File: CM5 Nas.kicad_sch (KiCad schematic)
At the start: 0 parts

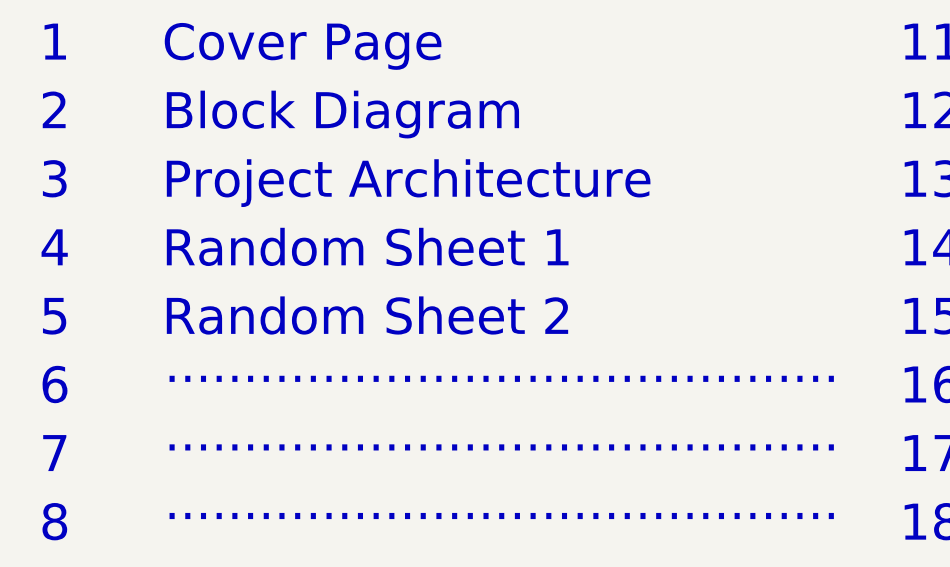
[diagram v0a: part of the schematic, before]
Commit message: Progress in power input and sata power option
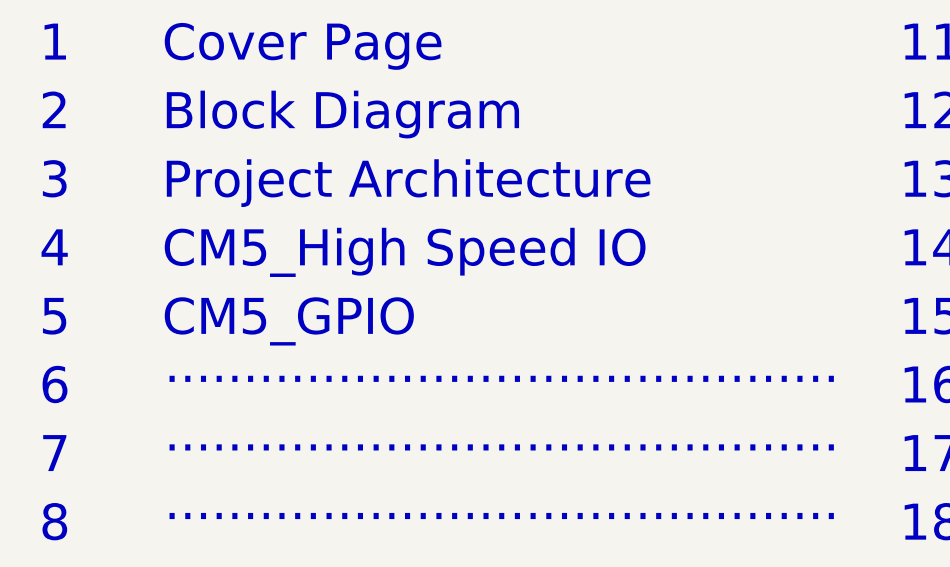
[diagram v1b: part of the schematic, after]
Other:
- note added: "CM5_GPIO"
- note added: "CM5_High Speed IO"
- note removed: "Random Sheet 1"
- note removed: "Random Sheet 2"
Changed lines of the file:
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@@
 		)
 	)
-	(text "Random Sheet 1"
+	(text "CM5_High Speed IO"
 		(exclude_from_sim no)
 		(at 45.72 106.68 0)
@@
 		)
 	)
-	(text "Random Sheet 2"
+	(text "CM5_GPIO"
 		(exclude_from_sim no)
 		(at 45.72 114.3 0)

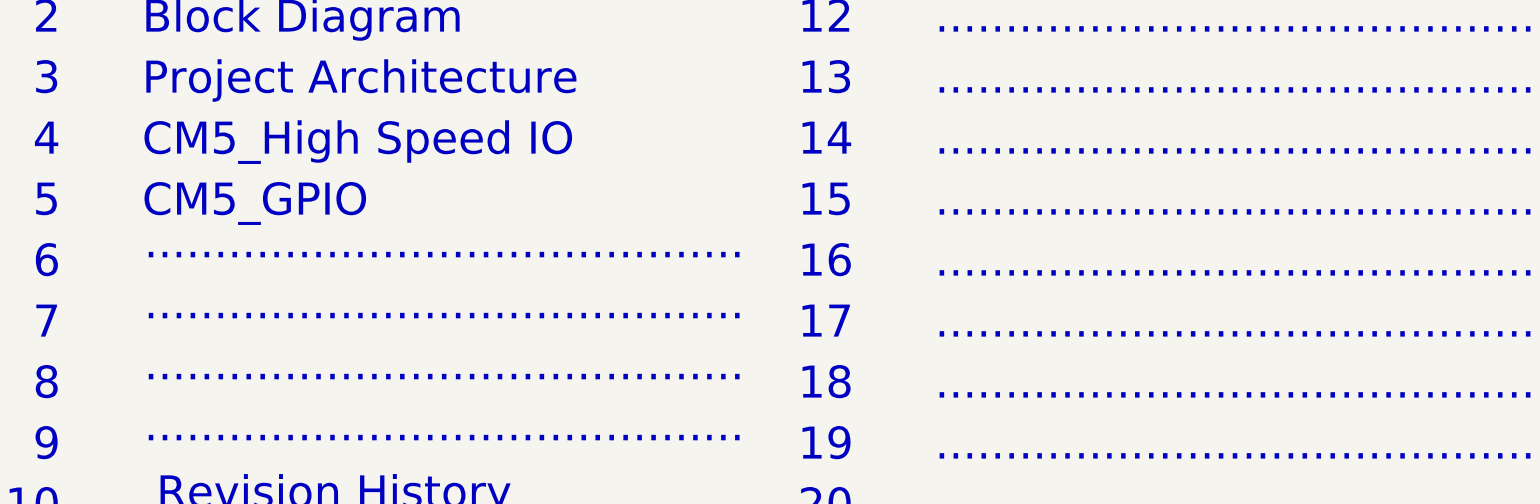
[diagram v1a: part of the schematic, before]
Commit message: Libaries added
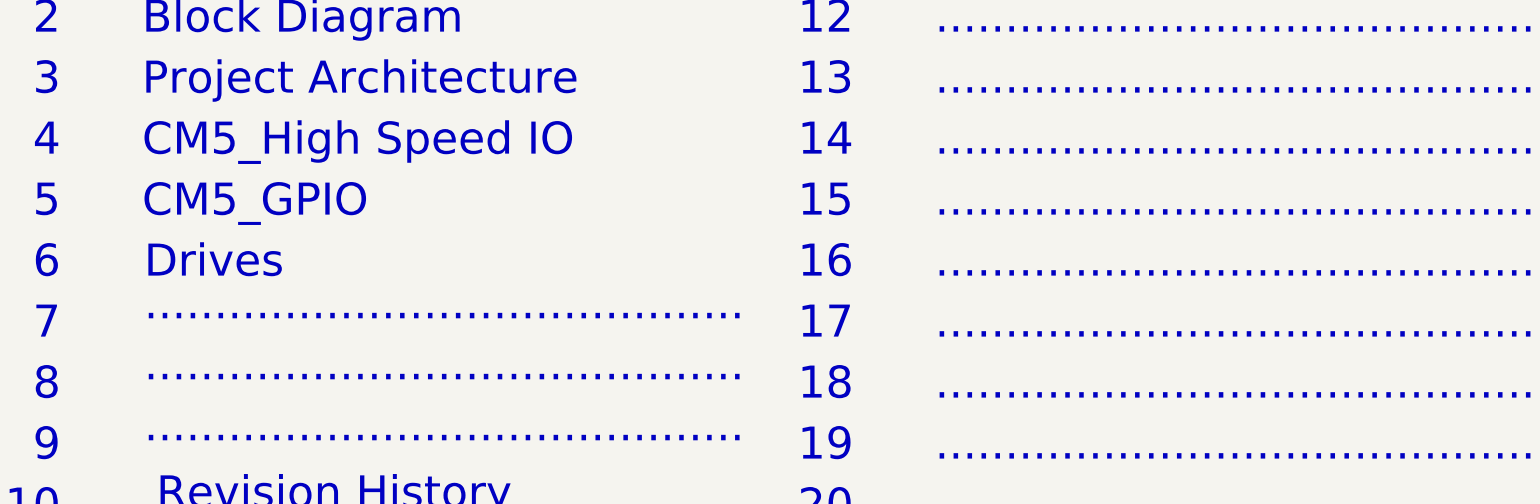
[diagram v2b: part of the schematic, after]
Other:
- note added: "Drives"
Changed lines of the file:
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@@
 		)
 	)
-	(text "..........................................."
+	(text "Drives"
 		(exclude_from_sim no)
-		(at 45.974 119.634 0)
+		(at 45.974 121.92 0)
 		(effects
 			(font
@@
 			)
 			(justify left bottom)
-			(href "#27")
+			(href "#6")
 		)
 	)

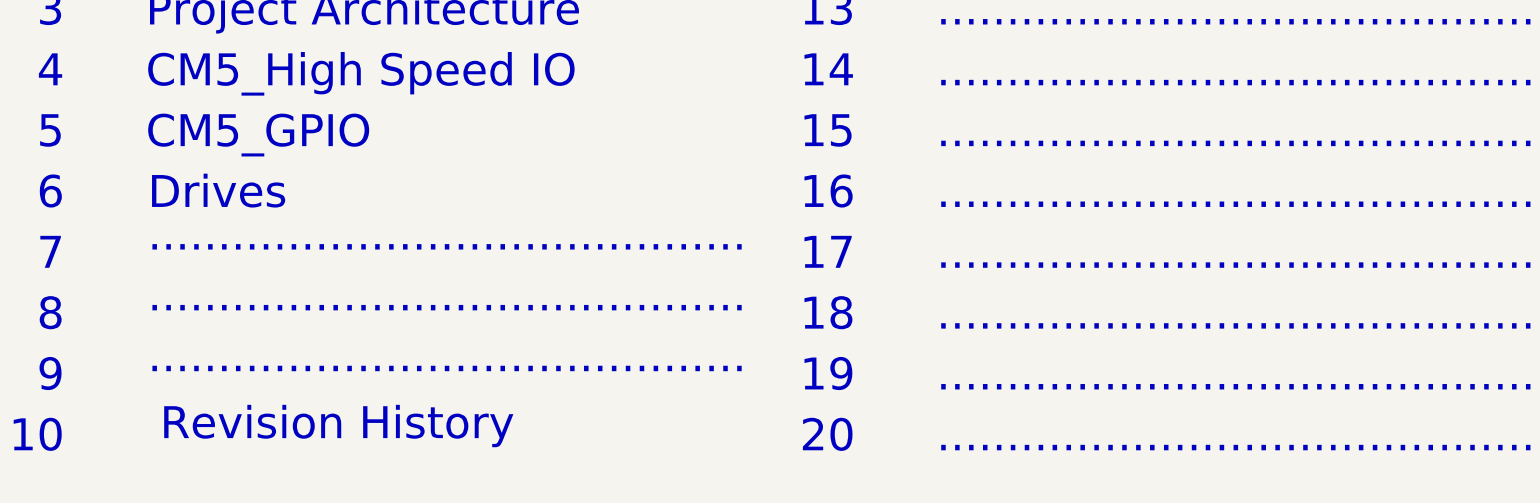
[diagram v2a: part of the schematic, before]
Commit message: Sheet name edit and changed to net labels
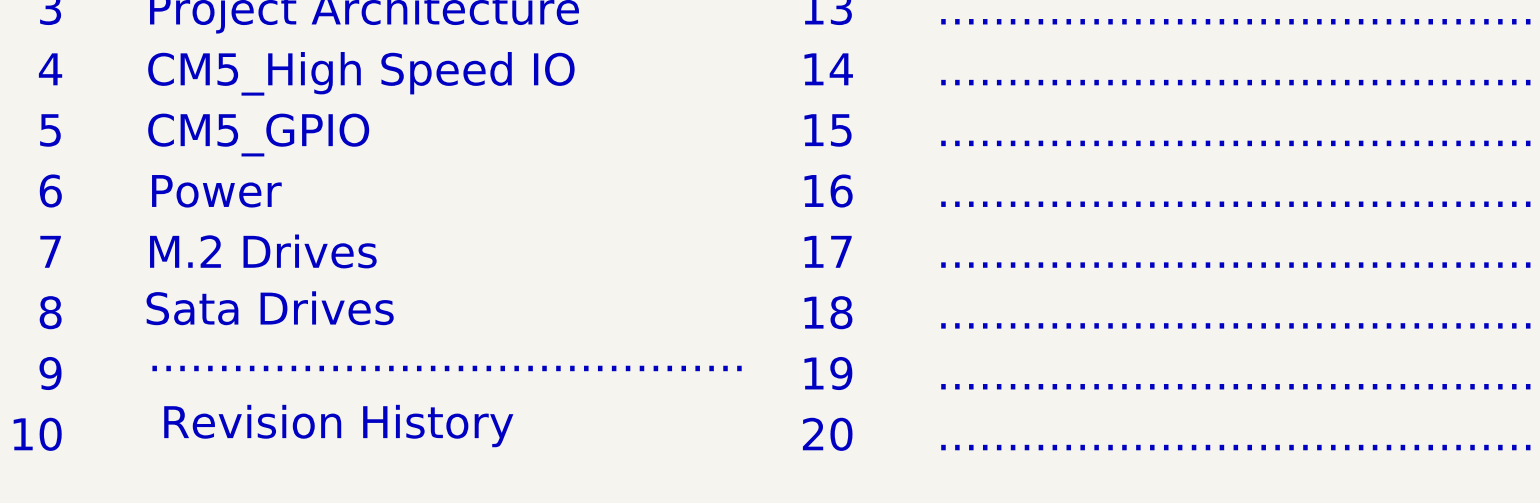
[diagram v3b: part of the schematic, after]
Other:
- note added: "M.2 Drives"
- note added: "Power"
- note added: "Sata Drives"
- note removed: "Drives"
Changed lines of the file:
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@@
 		)
 	)
-	(text "Drives"
+	(text "Power"
 		(exclude_from_sim no)
 		(at 45.974 121.92 0)
@@
 		)
 	)
+	(text "Sata Drives"
+		(exclude_from_sim no)
+		(at 45.466 136.652 0)
+		(effects
+			(font
+				(face "Times New Roman")
+				(size 4 4)
+				(color 0 0 0 1)
+			)
+			(justify left bottom)
+			(href "#8")
+		)
+	)
+	(text "CM5_GPIO"
+		(exclude_from_sim no)
+		(at 45.72 114.3 0)
+		(effects
+			(font
+				(face "Times New Roman")
+				(size 4 4)
+				(color 0 0 0 1)
+			)
+			(justify left bottom)
+			(href "#5")
+		)
+	)
 	(text "..........................................."
 		(exclude_from_sim no)
-		(at 45.974 134.874 0)
-		(effects
-			(font
-				(face "Times New Roman")
-				(size 4 4)
-				(color 0 0 0 1)
-			)
-			(justify left bottom)
-			(href "#29")
-		)
-	)
-	(text "CM5_GPIO"
-		(exclude_from_sim no)
-		(at 45.72 114.3 0)
-		(effects
-			(font
-				(face "Times New Roman")
-				(size 4 4)
-				(color 0 0 0 1)
-			)
-			(justify left bottom)
-			(href "#5")
+		(at 144.78 144.78 0)
+		(effects
+			(font
+				(face "Times New Roman")
+				(size 4 4)
+				(color 0 0 0 1)
+			)
+			(justify left bottom)
+			(href "#19")
 		)
 	)
 	(text "..........................................."
 		(exclude_from_sim no)
-		(at 144.78 144.78 0)
-		(effects
-			(font
-				(face "Times New Roman")
-				(size 4 4)
-				(color 0 0 0 1)
-			)
-			(justify left bottom)
-			(href "#19")
+		(at 144.78 83.82 0)
+		(effects
+			(font
+				(face "Times New Roman")
+				(size 4 4)
+				(color 0 0 0 1)
+			)
+			(justify left bottom)
+			(href "#11")
 		)
 	)
 	(text "..........................................."
 		(exclude_from_sim no)
-		(at 144.78 83.82 0)
-		(effects
-			(font
-				(face "Times New Roman")
-				(size 4 4)
-				(color 0 0 0 1)
-			)
-			(justify left bottom)
-			(href "#11")
-		)
-	)
-	(text "..........................................."
-		(exclude_from_sim no)
 		(at 144.78 129.54 0)
 		(effects
@@
 		)
 	)
-	(text "..........................................."
-		(exclude_from_sim no)
-		(at 45.974 127.254 0)
-		(effects
-			(font
-				(face "Times New Roman")
-				(size 4 4)
-				(color 0 0 0 1)
-			)
-			(justify left bottom)
-			(href "#28")
-		)
-	)
+	(text "M.2 Drives"
+		(exclude_from_sim no)
+		(at 45.72 129.54 0)
+		(effects
+			(font
+				(face "Times New Roman")
+				(size 4 4)
+				(color 0 0 0 1)
+			)
+			(justify left bottom)
+			(href "#7")
+		)
+	)

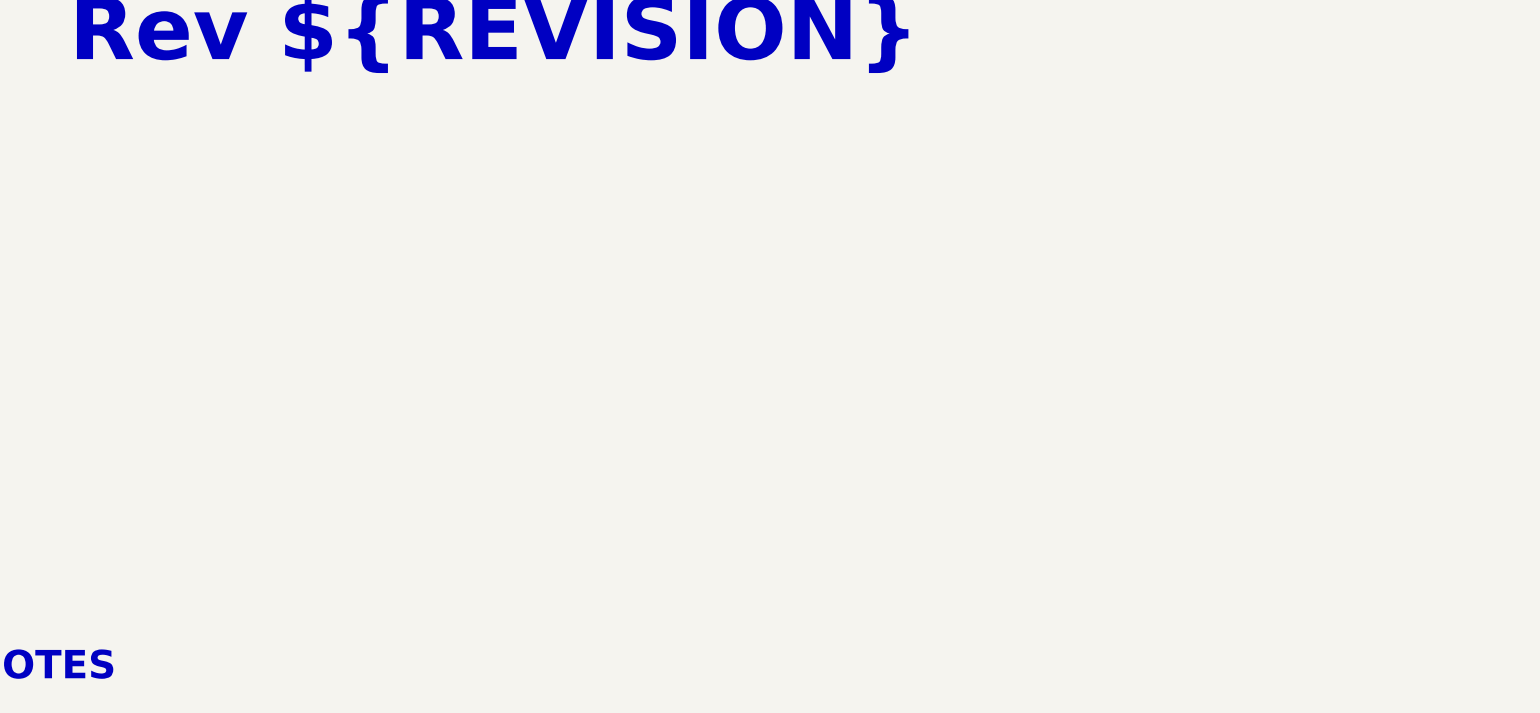
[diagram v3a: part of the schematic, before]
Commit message: Started Ethernet design
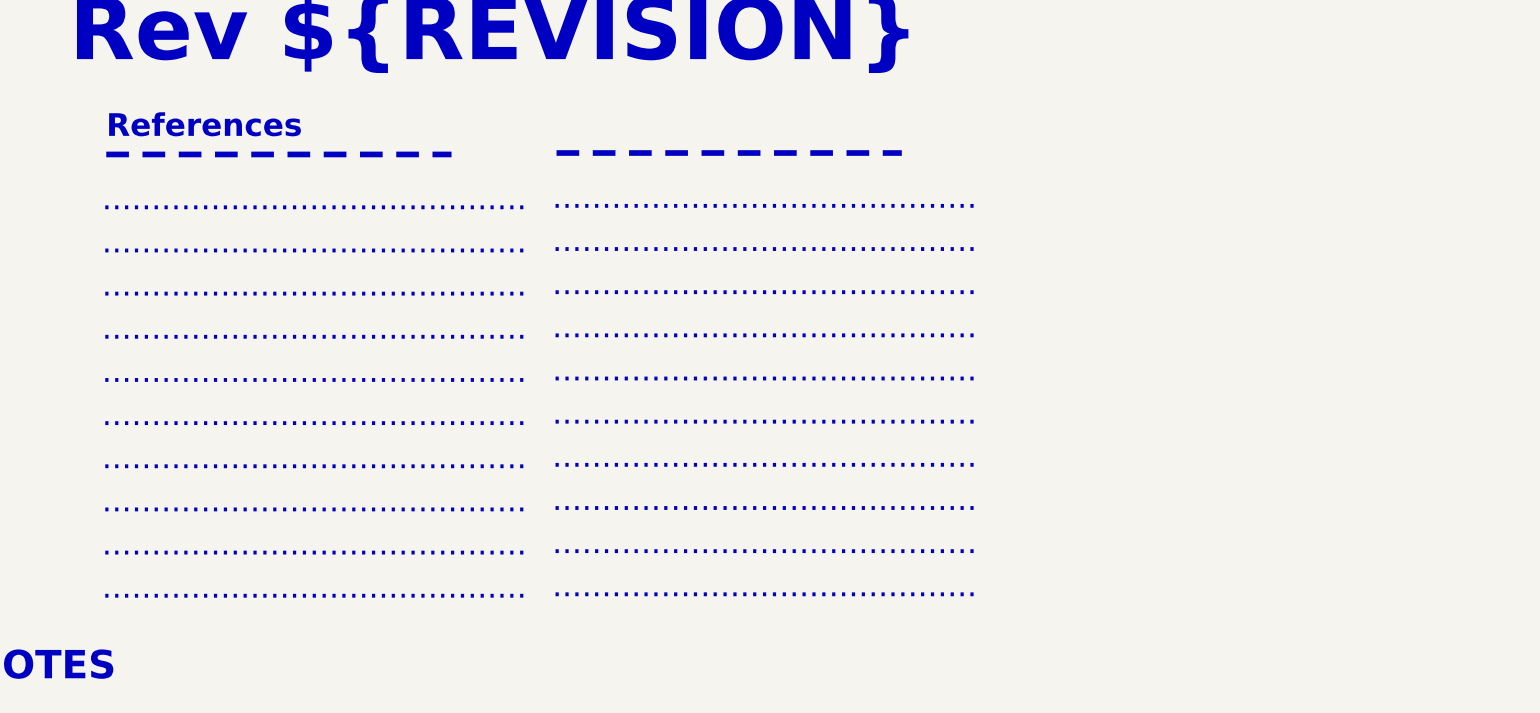
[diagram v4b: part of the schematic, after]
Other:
- note added: "References"

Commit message: Removed Ethernet
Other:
- note added: "Ethernet"
- note added: "Github CM5_NAS"
- note added: "Sata Drives 1"
- note added: "Sata Drives 2"
- note removed: "${VARIANT} ${RELEASE_DATE}"
- note removed: "Revision History"
- note removed: "Sata Drives"
- note removed: "Variant: ${VARIANT}"
